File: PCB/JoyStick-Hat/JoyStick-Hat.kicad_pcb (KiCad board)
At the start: 4 copper layers, 120 x 65 mm, 120 parts, among them J1 20021121-00010C4LF, J10 Conn_02x06_Odd_Even, J14 Conn_01x03_Pin, J15 Conn_01x03_Pin, J2 BU2032SM-JJ-GTR, J3 Conn_02x05_Odd_Even, J4 Conn_02x04_Odd_Even, J5 RJHSE-5381, J6 1757242, J7 Raspberry_Pi_2_3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

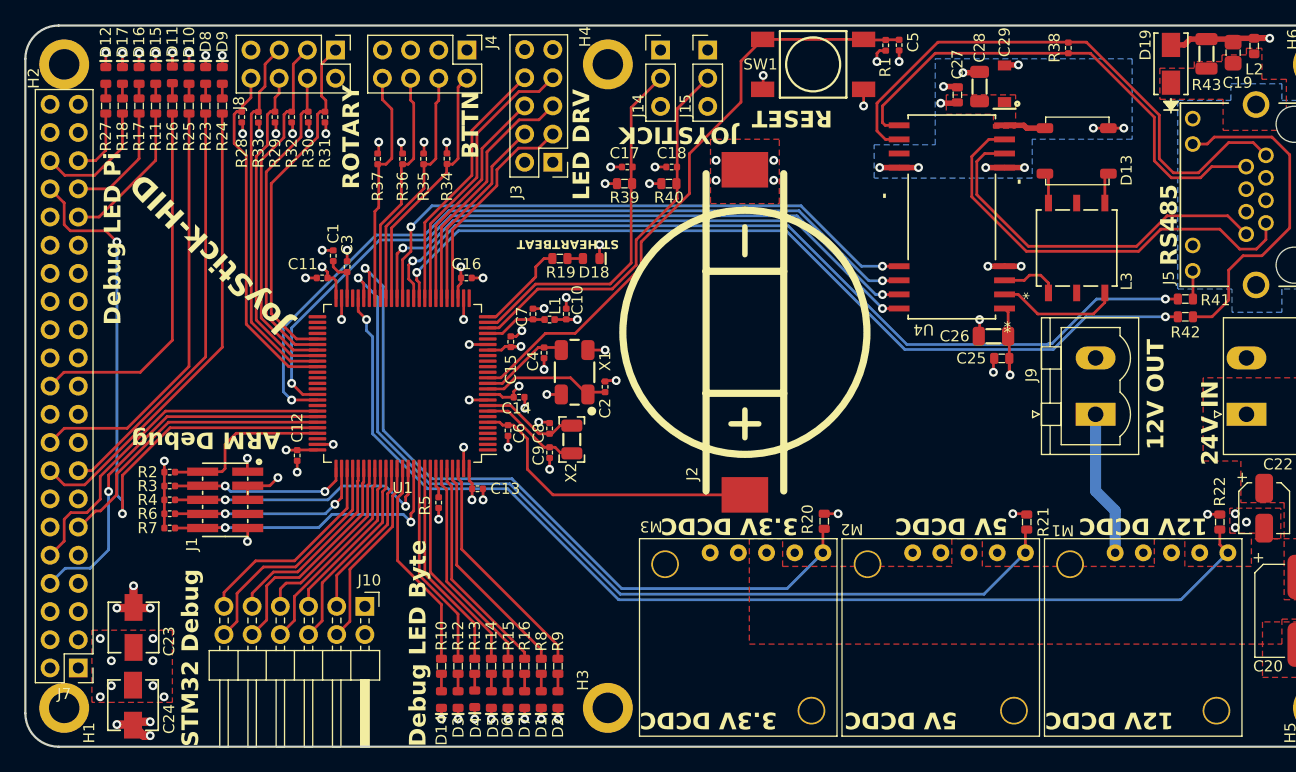
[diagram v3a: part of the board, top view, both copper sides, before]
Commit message: Silkscreen Tweaks
Added lots of labels to silkscreen and moved some traces
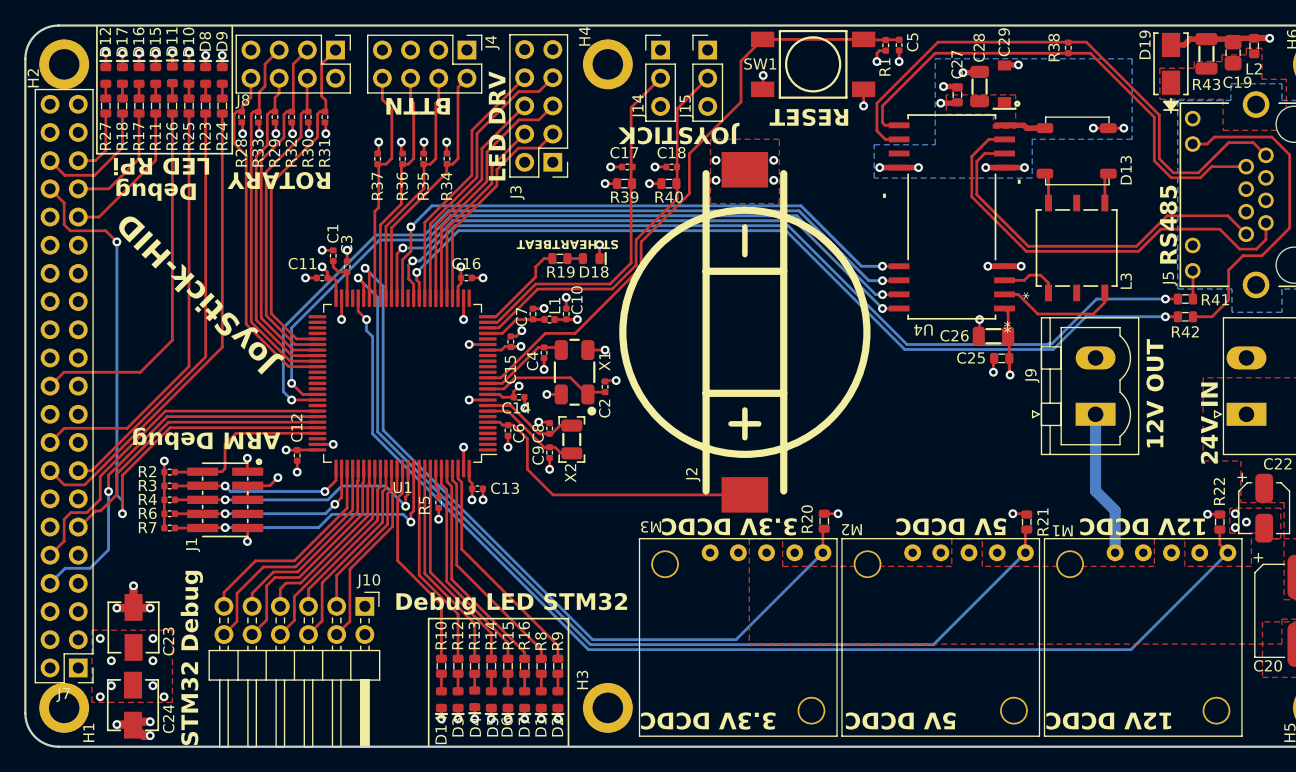
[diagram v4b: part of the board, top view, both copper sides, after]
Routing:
- net /Power/3.3V_PG: track 67.2 -> 71.0 mm
- net /Power/5V_PG: track 84.7 -> 88.5 mm
- net /Power/12V_PG: track 100.2 -> 103.9 mm
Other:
- board text added: "12V PG"
- board text added: "12V Rail"
- board text added: "24V"
- board text added: "24V Rail"
- board text added: "3V3 PG"
- board text added: "3V3 Rail"
- board text added: "5V PG"
- board text added: "5V Rail"
- board text added: "Debug"
- board text added: "Debug LED STM32"
- board text added: "GND"
- board text added: "GhostPCB LLC"
- board text added: "LED RPi"
- board text added: "PC10"
- board text added: "PC11"
- board text added: "PC12"
- board text added: "PD0"
- board text added: "PD1"
- board text added: "PD2"
- board text added: "PD3"
- board text added: "PD4"
- board text added: "PD5"
- board text added: "PD6"
- board text removed: "Debug LED Byte"
- board text removed: "Debug LED Pi"

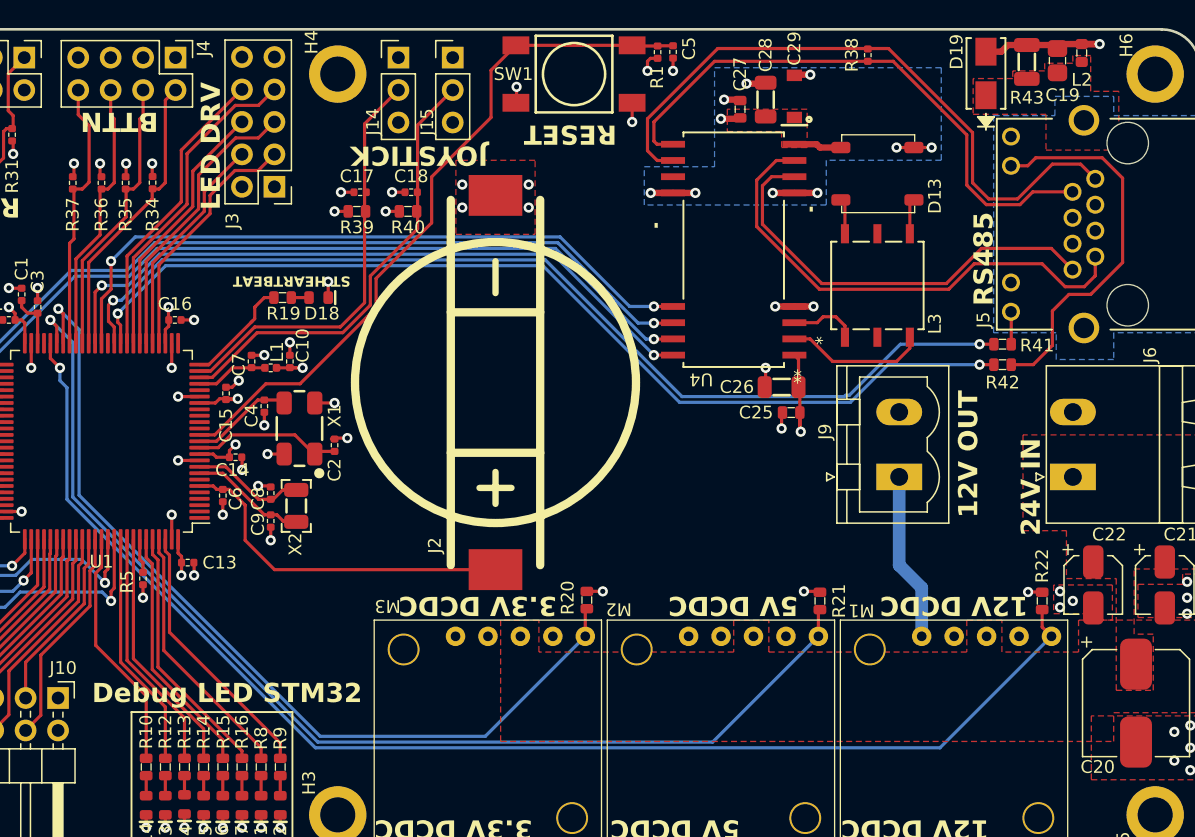
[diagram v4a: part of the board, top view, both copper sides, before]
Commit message: Connectors Moved, Labels Added, and New Images
Moved connectors around so labels can be fit on the bottom of PCB, labels added to bottom of PCB. New images exported !
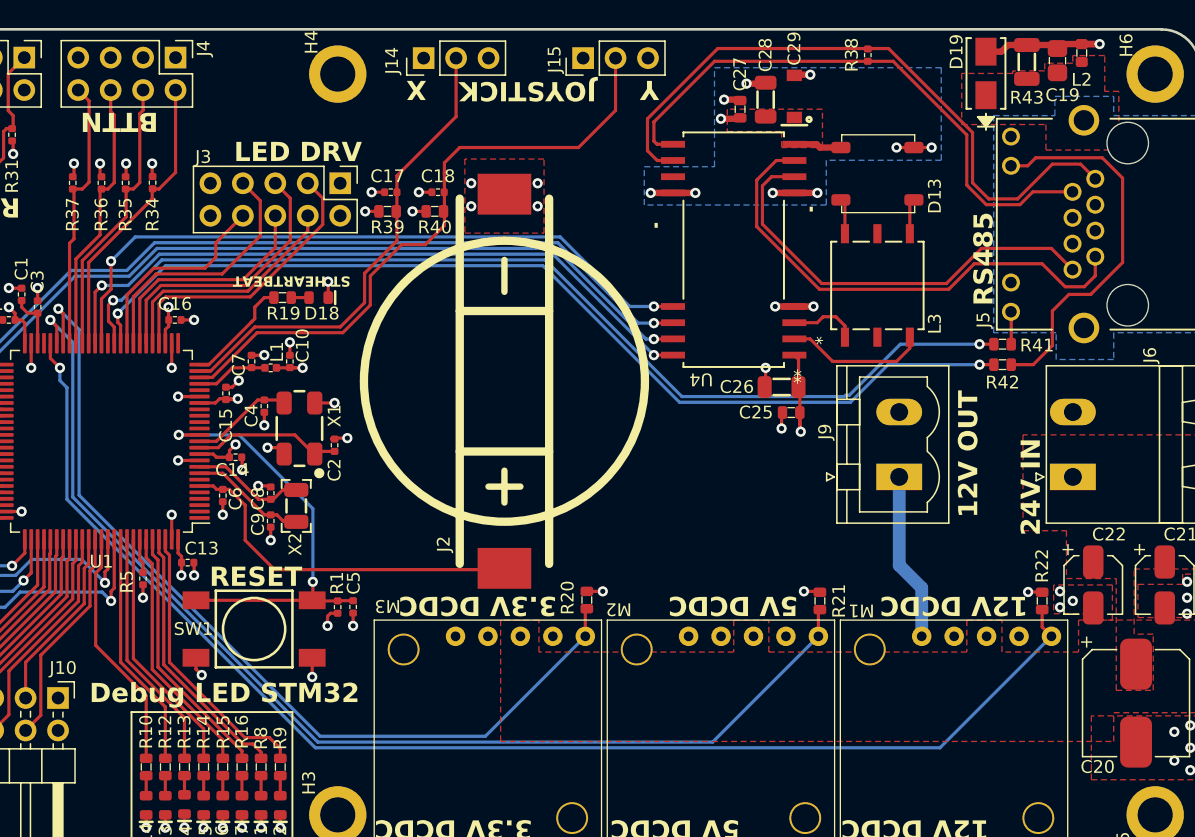
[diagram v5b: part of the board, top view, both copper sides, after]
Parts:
- moved SW1 50.2 mm to (145.7, 96.7)
- moved C5 50.2 mm to (153.4, 95.0)
- moved R1 50.2 mm to (152.2, 95.0)
- moved J15 10.2 mm to (171.5, 52.0), turned to 90 degrees
- moved J3 5.16 mm to (152.4, 61.8), turned to -90 degrees
- moved C17 2.40 mm to (156.4, 62.5)
- moved R39 2.40 mm to (156.2, 64.0)
- moved C18 2.10 mm to (160.1, 62.5)
- moved R40 2.10 mm to (159.8, 64.0)
- moved J14 1.98 mm to (159.0, 52.0), turned to 90 degrees
- moved J2 0.71 mm to (165.3, 77.3)
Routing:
- net GND: track 442.4 -> 87.7 mm
- net /STM32F446RET6-MCU/NRST: track 55.4 -> 34.2 mm, vias 0 -> 2
- net /JoyStick Interface/JOYSTICK_Y: track 35.2 -> 49.7 mm
- net /STM32F446RET6-MCU/LED_DRIVER_XLAT2: track 23.6 -> 16.1 mm
- net /STM32F446RET6-MCU/LED_DRIVER_BLANK: track 25.5 -> 20.2 mm
- net /JoyStick Interface/JOYSTICK_X: track 32.9 -> 37.3 mm
- net /STM32F446RET6-MCU/LED_DRIVER_XLAT: track 19.6 -> 22.2 mm
- net /STM32F446RET6-MCU/LED_DRIVER_MOSI: track 20.6 -> 18.3 mm
- net /STM32F446RET6-MCU/LED_DRIVER_SCLK: track 17.7 -> 18.9 mm
- net Net-(U1-PE1): track 20.9 -> 22.0 mm
- net /STM32F446RET6-MCU/LED_DRIVER_BLANK2: track 22.5 -> 21.6 mm
- net /STM32F446RET6-MCU/VBAT: track 27.8 -> 28.4 mm
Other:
- board text added: "3V3"
- board text added: "GND / PD13"
- board text added: "GND / PD8"
- board text added: "PA0"
- board text added: "PA1"
- board text added: "PA4"
- board text added: "PA5"
- board text added: "PA6"
- board text added: "PA7"
- board text added: "PC4"
- board text added: "PC5"
- board text added: "PD10 / PD9"
- board text added: "PD12 / PD11"
- board text added: "PE10"
- board text added: "PE11"
- board text added: "PE12"
- board text added: "PE9"
- board text added: "X"
- board text added: "Y"
